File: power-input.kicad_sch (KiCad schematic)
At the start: 21 parts, among them J204 Conn_01x02, J301 Conn_01x02, U202 XL1509-3.3

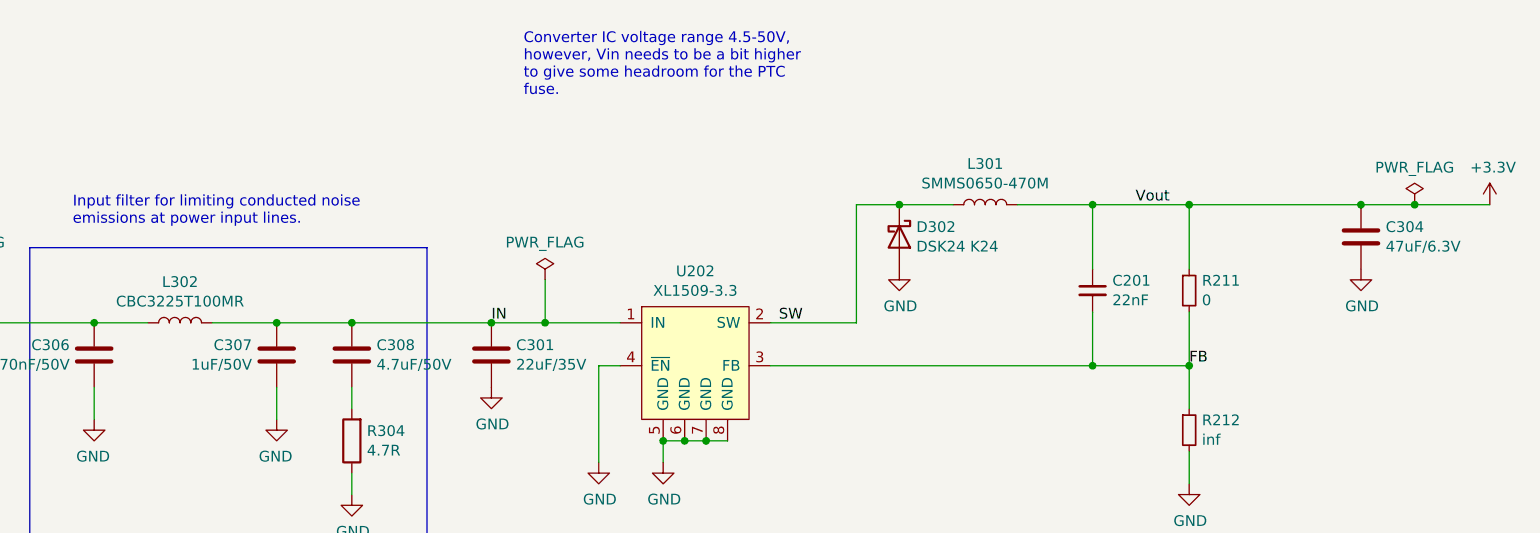
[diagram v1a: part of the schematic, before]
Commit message: Go back to ISO1050 for CAN transceiver
Also add CAN RX and TX LEDs and beef up buck capacitors
as much as space allows.
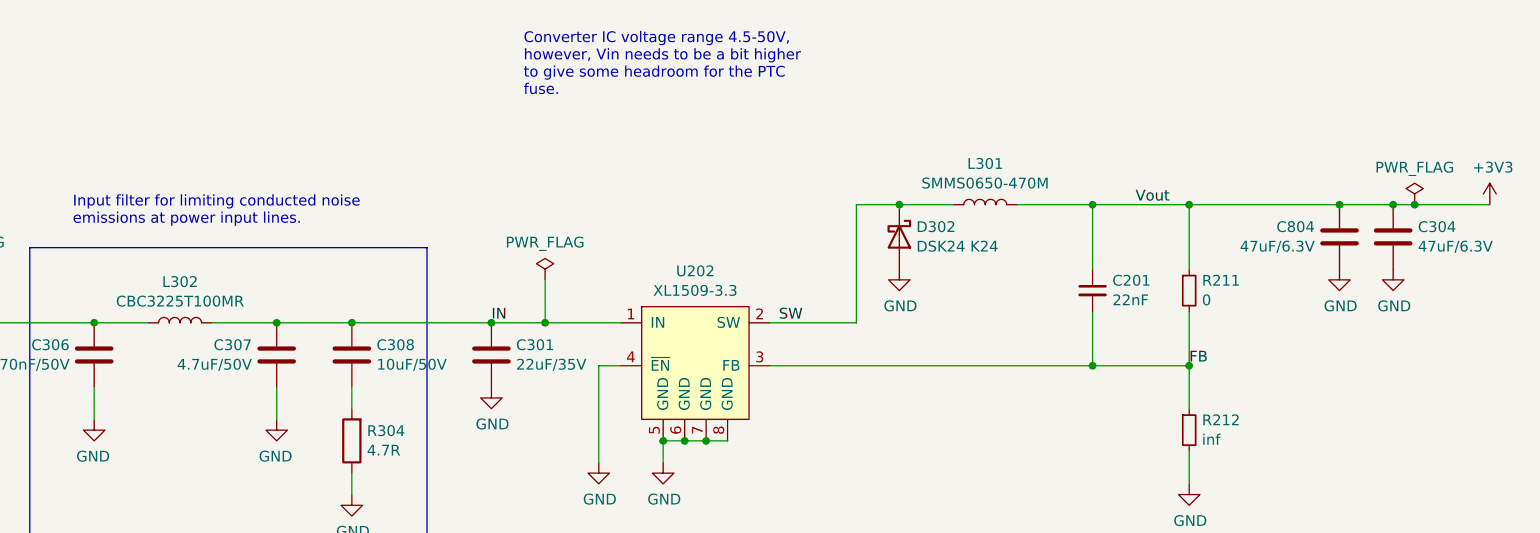
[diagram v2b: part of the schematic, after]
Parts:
- added C804: 47uF/6.3V, Capacitor_SMD:C_1206_3216Metric, symbol Device:C
- C301: footprint Capacitor_SMD:C_1206_3216Metric -> Capacitor_SMD:C_1210_3225Metric
- C307: value 1uF/50V -> 4.7uF/50V; LCSC C28323 -> C2991173
- C308: value 4.7uF/50V -> 10uF/50V; LCSC C29823 -> C89632
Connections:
- net +3V3: now also C804.1
- net GND: now also C804.2
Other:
- company: Hat Labs Ltd -> Hat Labs Oy
- title: Sailor Hat with ESP32 -> SH-ESP32
- moved on the sheet: C304

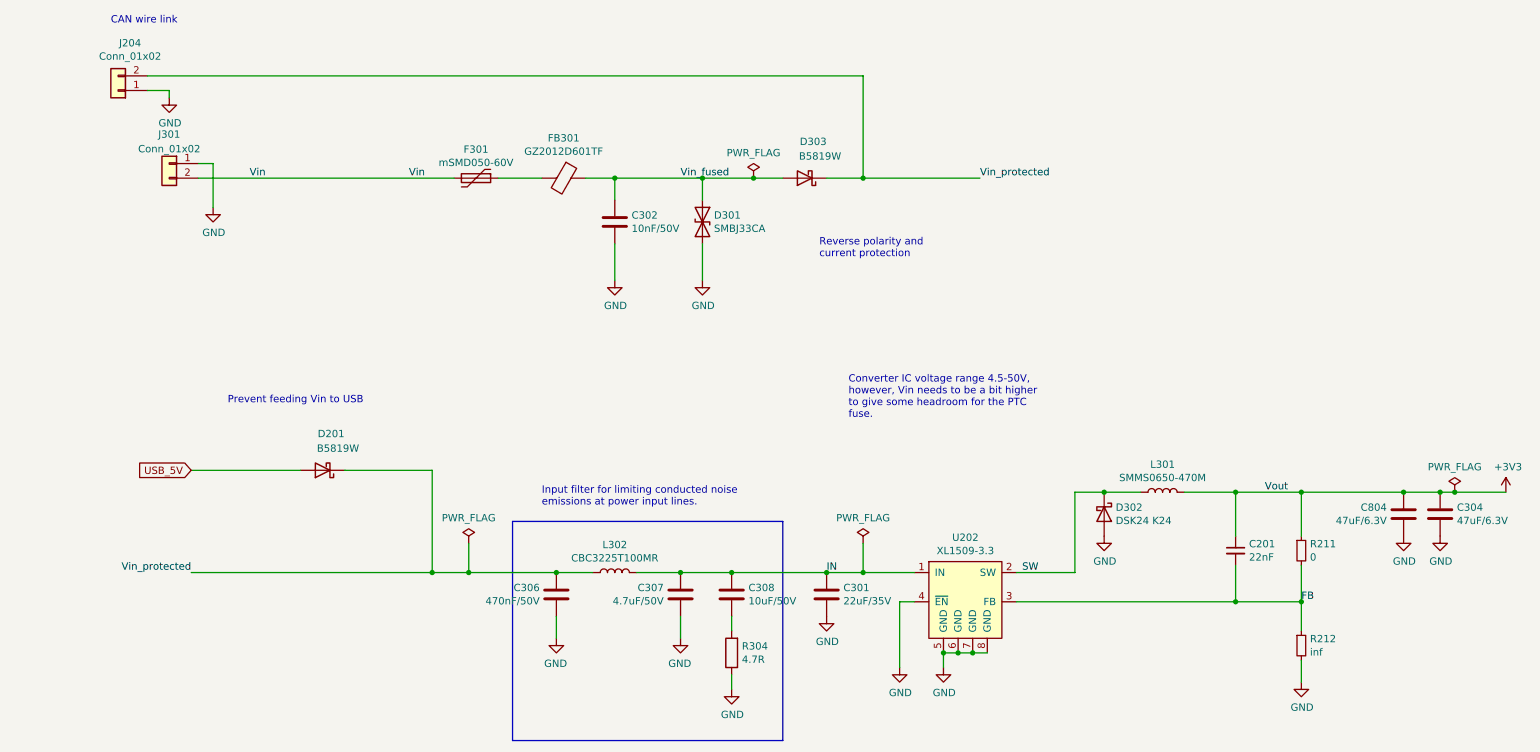
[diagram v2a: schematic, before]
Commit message: Change buck converter to LMR54410
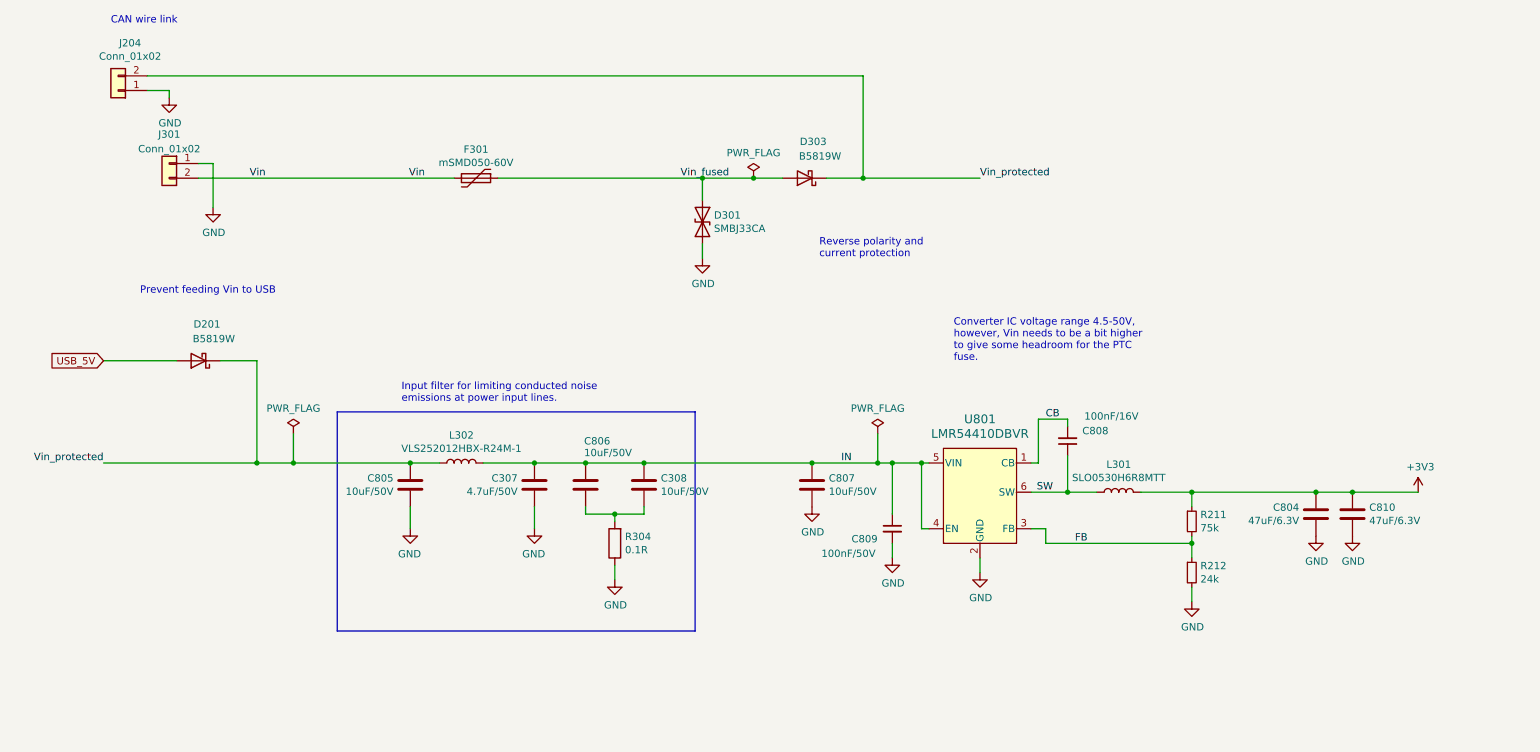
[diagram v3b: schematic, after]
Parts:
- removed C201: 22nF, Capacitor_SMD:C_0402_1005Metric, symbol Device:C_Small
- removed C301: 22uF/35V, Capacitor_SMD:C_1210_3225Metric, symbol Device:C
- removed C302: 10nF/50V, Capacitor_SMD:C_0402_1005Metric, symbol Device:C
- removed C304: 47uF/6.3V, Capacitor_SMD:C_1206_3216Metric, symbol Device:C
- removed C306: 470nF/50V, Capacitor_SMD:C_0805_2012Metric, symbol Device:C
- removed D302: DSK24 K24, Diode_SMD:D_SOD-123F, symbol Device:D_Schottky
- removed FB301: GZ2012D601TF, Inductor_SMD:L_0805_2012Metric, symbol Device:FerriteBead
- removed U202: XL1509-3.3, Package_SO:SOP-8_3.9x4.9mm_P1.27mm, symbol SH-ESP32:XL1509-ADJE1
- added C805, C806, C807: 10uF/50V, Capacitor_SMD:C_1206_3216Metric, symbol Device:C
- added C808: 100nF/16V, Capacitor_SMD:C_0402_1005Metric, symbol Device:C_Small
- added C809: 100nF/50V, Capacitor_SMD:C_0603_1608Metric, symbol Device:C_Small
- added C810: 47uF/6.3V, Capacitor_SMD:C_0805_2012Metric, symbol Device:C
- added U801: LMR54410DBVR, SOT-23-6-DBV_TEX, symbol SH-ESP32:LMR54410DBVR
- C308: LCSC C89632 -> C13585
- C804: footprint Capacitor_SMD:C_1206_3216Metric -> Capacitor_SMD:C_0805_2012Metric; LCSC C96123 -> C16780
- L301: value SMMS0650-470M -> SLO0530H6R8MTT; footprint SH-ESP32:SMMS0650-1R0M -> Inductor_SMD:L_Chilisin_BMRA00050530; LCSC C149588 -> C325965
- L302: value CBC3225T100MR -> VLS252012HBX-R24M-1
- R211: value 0 -> 75k; LCSC C17168 -> C208939
- R212: value inf -> 24k; LCSC (none) -> C25769
- R304: value 4.7R -> 0.1R; LCSC C23164 -> C3013345
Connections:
- net +3V3: now also C810.1
- net FB: now also U801.3 (FB)
- net GND: now also C805.2, C807.2, C809.2, C810.2, U801.2 (GND)
- net IN: now also C806.1, C807.1, C809.1, U801.4 (EN), U801.5 (VIN)
- net SW: now also C808.1, U801.6 (SW)
- net Vin_fused: now also F301.1
- net Vin_protected: now also C805.1
- net at C308.2, R304.2: now also C806.2
- new net CB: C808.2, U801.1 (CB)
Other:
- moved on the sheet: C307, C308, C804, D201, L301, L302, R211, R212, R304

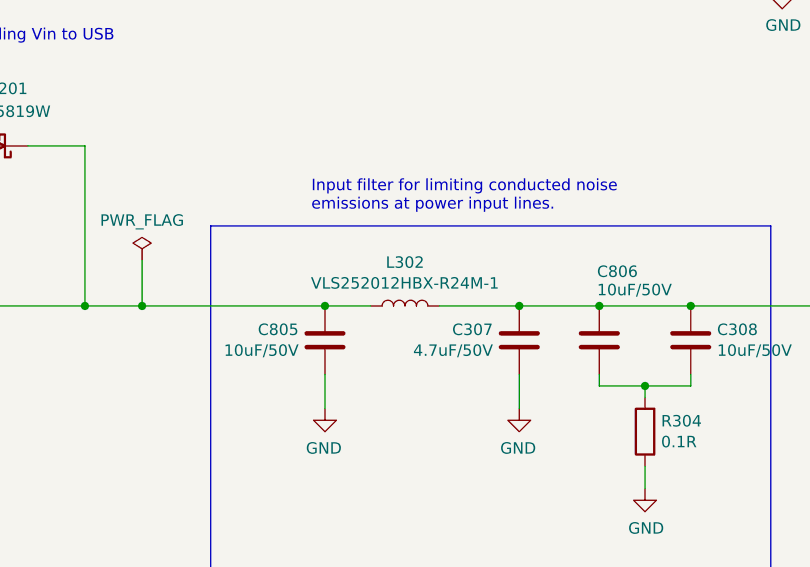
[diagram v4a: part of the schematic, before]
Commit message: Adjust parts according to availability
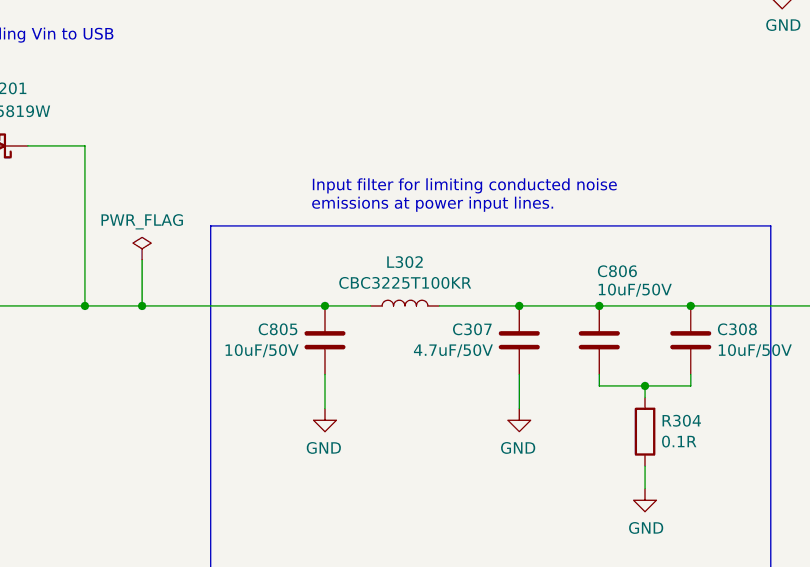
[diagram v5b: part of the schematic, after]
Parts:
- L302: value VLS252012HBX-R24M-1 -> CBC3225T100KR; LCSC C90315 -> C90321; Notes Alternatives: CBC3225T100KR, NLCV32T-100K-PFR -> Alternatives: CBC3225T100KR, CBC3225T100MR, NLCV32T-100K-PFR
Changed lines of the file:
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@@
 			)
 		)
-		(property "Value" "VLS252012HBX-R24M-1"
+		(property "Value" "CBC3225T100KR"
 			(at 95.25 100.3554 90)
 			(effects
@@
 			)
 		)
-		(property "LCSC" "C90315"
+		(property "LCSC" "C90321"
 			(at 95.25 102.87 0)
 			(effects
@@
 			)
 		)
-		(property "Notes" "Alternatives: CBC3225T100KR, NLCV32T-100K-PFR"
+		(property "Notes" "Alternatives: CBC3225T100KR, CBC3225T100MR, NLCV32T-100K-PFR"
 			(at 95.25 102.87 90)
 			(effects
